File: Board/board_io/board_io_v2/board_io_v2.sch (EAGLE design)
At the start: 38 parts, among them IC1 LD117AS33TR, IC2 LD117AS18TR, IC3 FT232RL

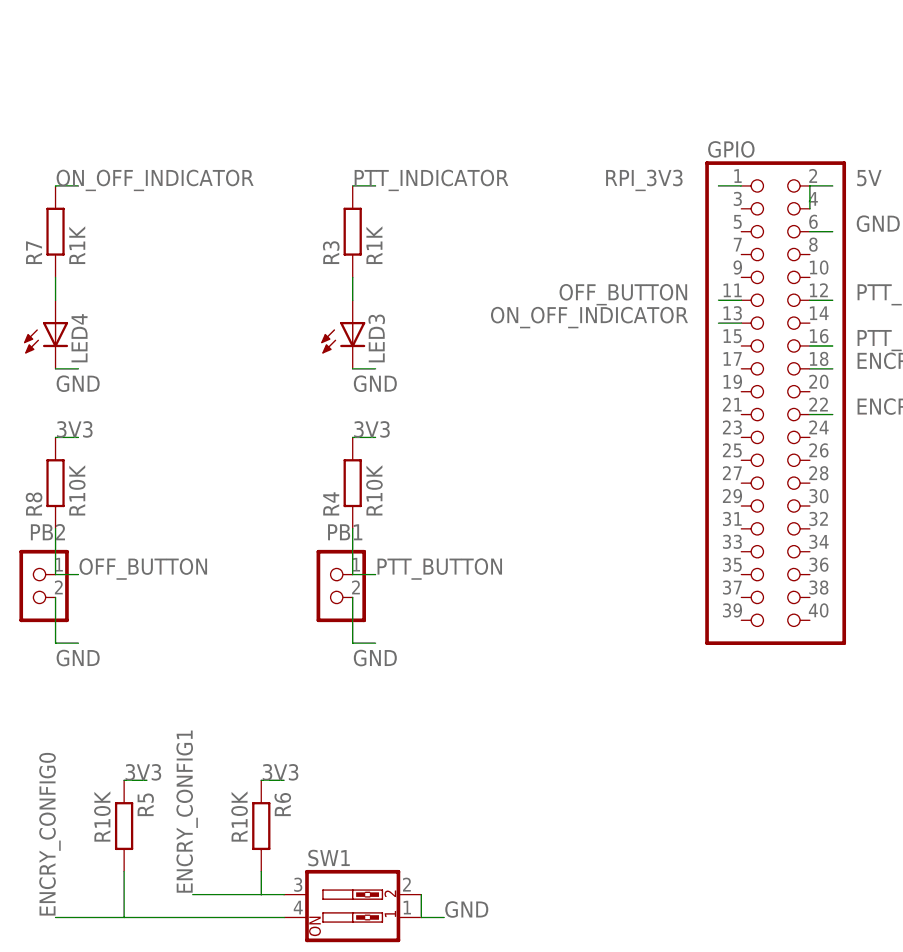
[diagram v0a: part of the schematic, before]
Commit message: update io board and add interface code
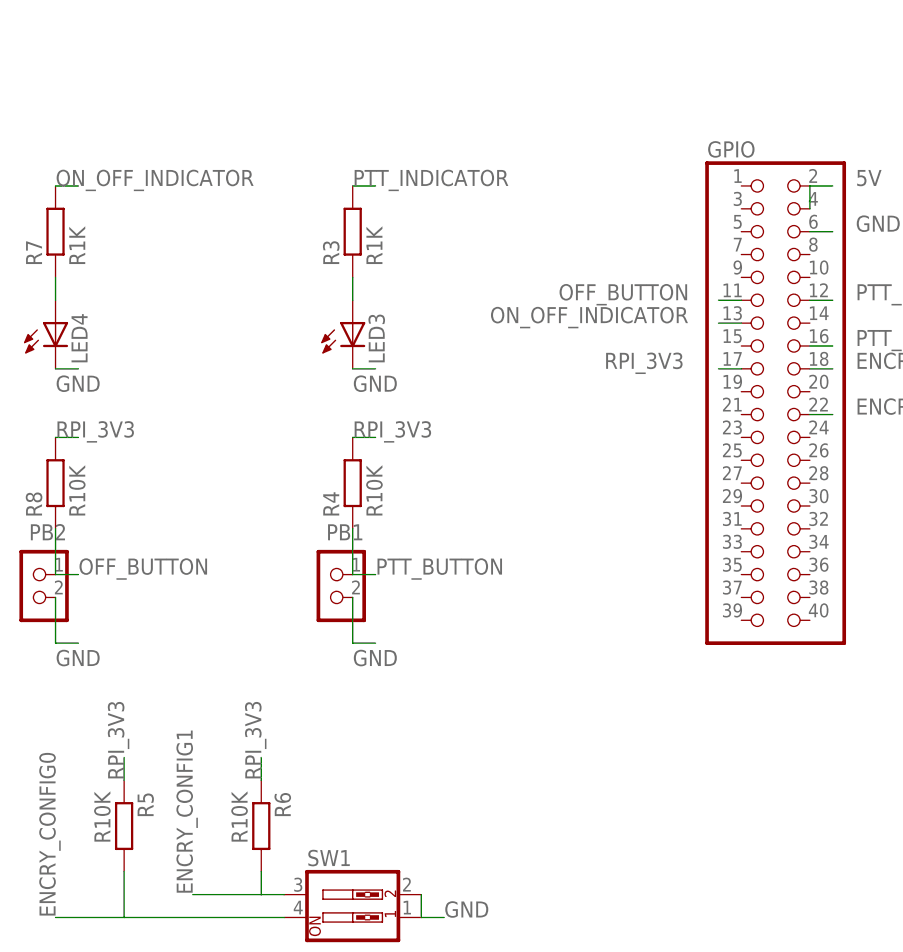
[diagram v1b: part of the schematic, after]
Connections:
- net 3V3: no longer R4.2, R5.1, R6.1, R8.2
- net RPI_3V3: now also GPIO.17, R4.2, R5.1, R6.1, R8.2; no longer GPIO.1
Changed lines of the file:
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@@
 <label x="213.36" y="15.24" size="1.778" layer="95"/>
-</segment>
-<segment>
-<pinref part="R4" gate="G$1" pin="2"/>
-<wire x1="-25.4" y1="27.94" x2="-22.86" y2="27.94" width="0.1524" layer="91"/>
-<label x="-25.4" y="27.94" size="1.778" layer="95"/>
-</segment>
-<segment>
-<pinref part="R6" gate="G$1" pin="1"/>
-<wire x1="-35.56" y1="-10.16" x2="-33.02" y2="-10.16" width="0.1524" layer="91"/>
-<label x="-35.56" y="-10.16" size="1.778" layer="95"/>
-</segment>
-<segment>
-<pinref part="R5" gate="G$1" pin="1"/>
-<wire x1="-50.8" y1="-10.16" x2="-48.26" y2="-10.16" width="0.1524" layer="91"/>
-<label x="-50.8" y="-10.16" size="1.778" layer="95"/>
-</segment>
-<segment>
-<pinref part="R8" gate="G$1" pin="2"/>
-<wire x1="-58.42" y1="27.94" x2="-55.88" y2="27.94" width="0.1524" layer="91"/>
-<label x="-58.42" y="27.94" size="1.778" layer="95"/>
 </segment>
 </net>
@@
 <net name="RPI_3V3" class="0">
 <segment>
-<pinref part="GPIO" gate="A" pin="1"/>
-<wire x1="17.78" y1="55.88" x2="15.24" y2="55.88" width="0.1524" layer="91"/>
-<label x="2.54" y="55.88" size="1.778" layer="95"/>
+<pinref part="R8" gate="G$1" pin="2"/>
+<wire x1="-58.42" y1="27.94" x2="-55.88" y2="27.94" width="0.1524" layer="91"/>
+<label x="-58.42" y="27.94" size="1.778" layer="95"/>
+</segment>
+<segment>
+<pinref part="R4" gate="G$1" pin="2"/>
+<wire x1="-25.4" y1="27.94" x2="-22.86" y2="27.94" width="0.1524" layer="91"/>
+<label x="-25.4" y="27.94" size="1.778" layer="95"/>
+</segment>
+<segment>
+<pinref part="R5" gate="G$1" pin="1"/>
+<wire x1="-50.8" y1="-10.16" x2="-50.8" y2="-7.62" width="0.1524" layer="91"/>
+<label x="-50.8" y="-10.16" size="1.778" layer="95" rot="R90"/>
+</segment>
+<segment>
+<pinref part="R6" gate="G$1" pin="1"/>
+<wire x1="-35.56" y1="-10.16" x2="-35.56" y2="-7.62" width="0.1524" layer="91"/>
+<label x="-35.56" y="-10.16" size="1.778" layer="95" rot="R90"/>
+</segment>
+<segment>
+<pinref part="GPIO" gate="A" pin="17"/>
+<wire x1="17.78" y1="35.56" x2="15.24" y2="35.56" width="0.1524" layer="91"/>
+<label x="2.54" y="35.56" size="1.778" layer="95"/>
 </segment>
 </net>
